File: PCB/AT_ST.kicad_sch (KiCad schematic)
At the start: 80 parts, among them J1 4PIN, J2 OLED, J3 Conn_01x05_Female, J4 Conn_01x05_Female, SW1 SW1, SW10 SW10, SW11 SW11, SW12 SW12, SW13 SW13, SW14 SW14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

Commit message: Updated some footprints.
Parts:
- R1, R2: footprint SofleKeyboard-footprint:R_1206_DoubleSided -> jw_custom_footprint:R_1206_DoubleSided
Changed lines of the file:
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@@
-    (stroke (width 0) (type default) (color 0 0 0 0))
-  )
-  (wire (pts (xy 42.418 71.628) (xy 42.418 73.787))
     (stroke (width 0) (type default) (color 0 0 0 0))
   )
@@
     (stroke (width 0) (type default) (color 0 0 0 0))
   )
+  (wire (pts (xy 42.418 71.628) (xy 46.99 71.628))
+    (stroke (width 0) (type default) (color 0 0 0 0))
+  )
   (wire (pts (xy 157.734 111.252) (xy 159.512 111.252))
     (stroke (width 0) (type default) (color 0 0 0 0))
@@
   )
   (wire (pts (xy 26.924 125.476) (xy 26.924 131.064))
+    (stroke (width 0) (type default) (color 0 0 0 0))
+  )
+  (wire (pts (xy 46.99 71.628) (xy 46.99 73.66))
     (stroke (width 0) (type default) (color 0 0 0 0))
   )
@@
     )
     (property "Value" "R" (id 1) (at 33.528 87.376 90))
-    (property "Footprint" "SofleKeyboard-footprint:R_1206_DoubleSided" (id 2) (at 33.528 85.598 90)
+    (property "Footprint" "jw_custom_footprint:R_1206_DoubleSided" (id 2) (at 33.528 85.598 90)
       (effects (font (size 1.27 1.27)) hide)
     )
@@
     )
     (property "Value" "R" (id 1) (at 33.528 82.804 90))
-    (property "Footprint" "SofleKeyboard-footprint:R_1206_DoubleSided" (id 2) (at 33.528 81.026 90)
+    (property "Footprint" "jw_custom_footprint:R_1206_DoubleSided" (id 2) (at 33.528 81.026 90)
       (effects (font (size 1.27 1.27)) hide)
     )
@@
     (pin "2")
   )
-  (symbol (lib_id "power:GND") (at 42.418 73.787 0) (unit 1)
-    (in_bom yes) (on_board yes)
-    (property "Reference" "#PWR0102" (id 0) (at 42.418 80.137 0)
-      (effects (font (size 1.27 1.27)) hide)
-    )
-    (property "Value" "GND" (id 1) (at 42.545 78.1812 0))
-    (property "Footprint" "" (id 2) (at 42.418 73.787 0)
-      (effects (font (size 1.27 1.27)) hide)
-    )
-    (property "Datasheet" "" (id 3) (at 42.418 73.787 0)
+  (symbol (lib_id "power:GND") (at 46.99 73.66 0) (unit 1)
+    (in_bom yes) (on_board yes)
+    (property "Reference" "#PWR0102" (id 0) (at 46.99 80.01 0)
+      (effects (font (size 1.27 1.27)) hide)
+    )
+    (property "Value" "GND" (id 1) (at 47.117 78.0542 0))
+    (property "Footprint" "" (id 2) (at 46.99 73.66 0)
+      (effects (font (size 1.27 1.27)) hide)
+    )
+    (property "Datasheet" "" (id 3) (at 46.99 73.66 0)
       (effects (font (size 1.27 1.27)) hide)
     )
@@
     )
     (path "/4f0dde52-9bad-44d4-aea8-222c0fca6124"
-      (reference "R1") (unit 1) (value "R") (footprint "SofleKeyboard-footprint:R_1206_DoubleSided")
+      (reference "R1") (unit 1) (value "R") (footprint "jw_custom_footprint:R_1206_DoubleSided")
     )
     (path "/401292cb-be96-4cb2-9cd9-a9fdf728011b"
-      (reference "R2") (unit 1) (value "R") (footprint "SofleKeyboard-footprint:R_1206_DoubleSided")
+      (reference "R2") (unit 1) (value "R") (footprint "jw_custom_footprint:R_1206_DoubleSided")
     )
     (path "/00000000-0000-0000-0000-00005b8ce7e7"

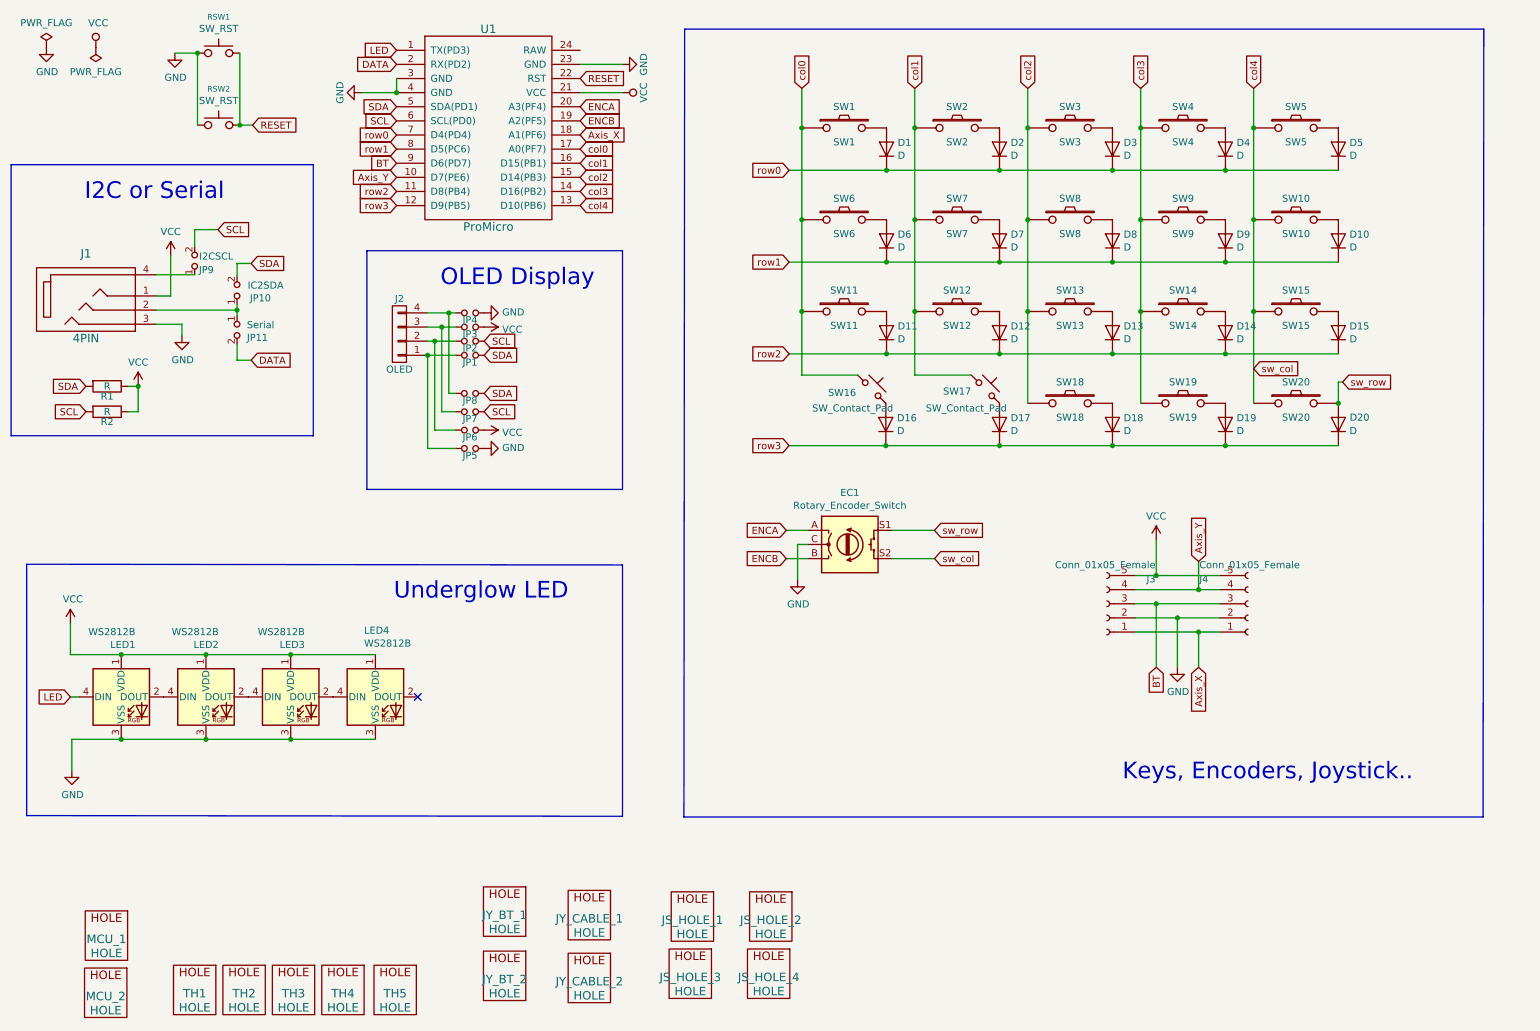
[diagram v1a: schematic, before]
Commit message: 1. Correct a serious pin allocation problem, where a digital pin was assigned for joystick Y axis. 2. Updated MX switches footprints. 3. Included flip style 5 pins FPC/FFC socket. 4. Minor changes here and there.
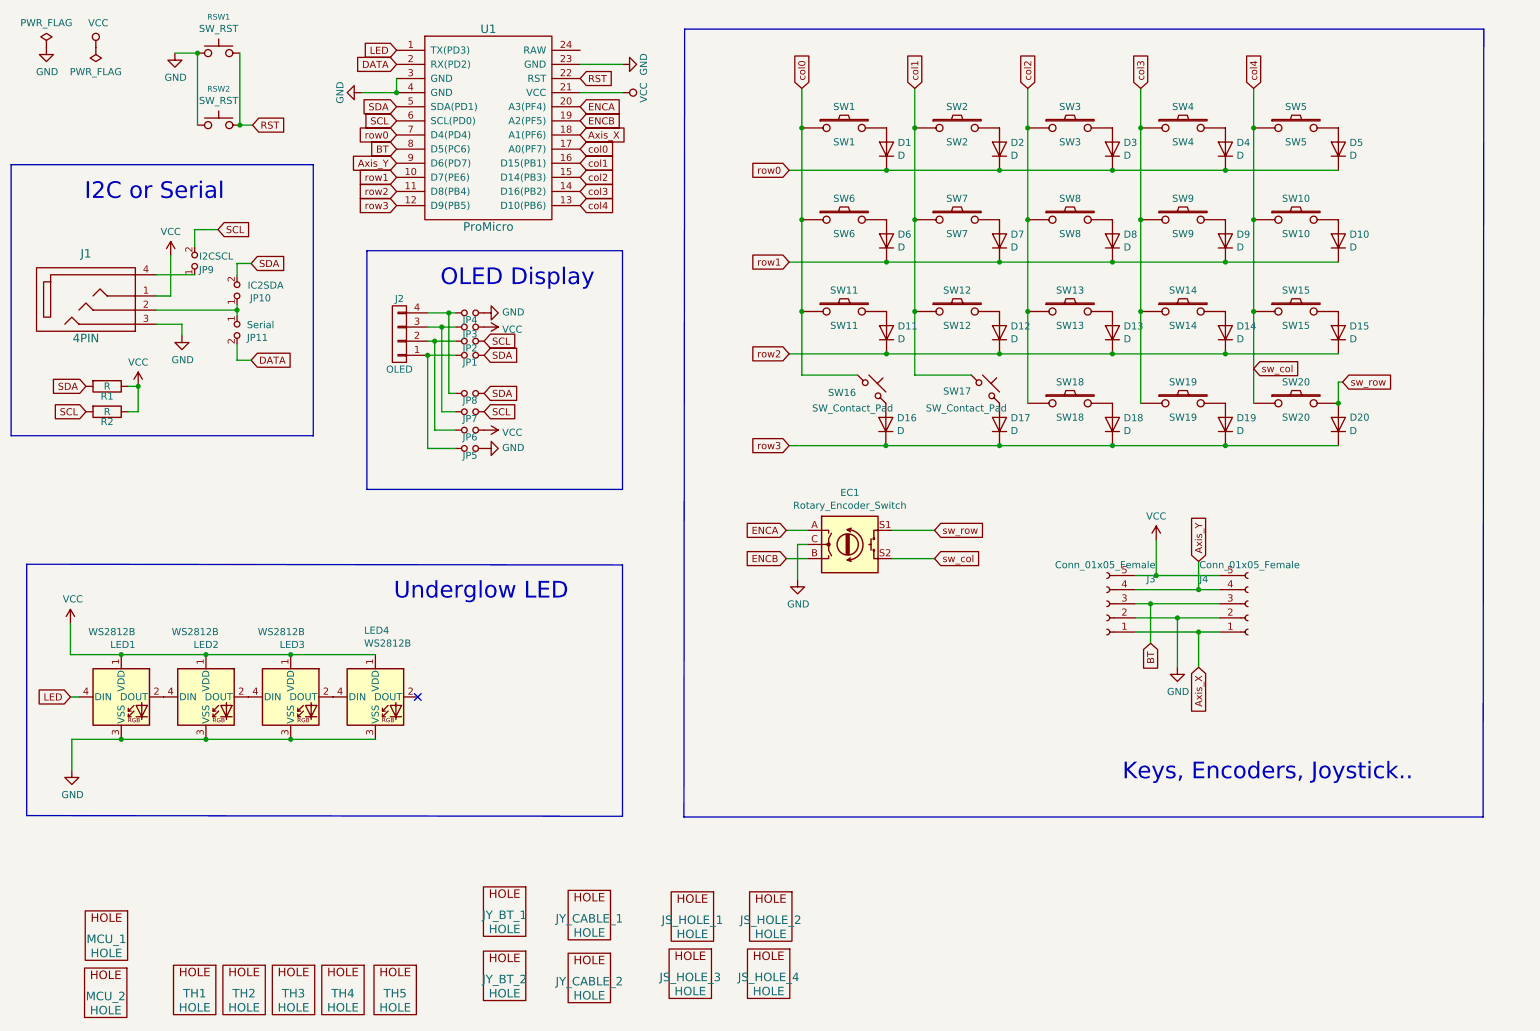
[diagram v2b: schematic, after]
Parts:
- D1, D10, D11, D12, D13, D14, D15, D16, D17, D18, D19, D2, D20, D3, D4, D5, D6, D7, D8, D9: footprint jw_custom_footprint:Diode_SOD123_THT -> jw_custom_footprint:Diode_SOD123_THT_2
- J3, J4: footprint Connector_FFC-FPC:TE_0-1734839-5_1x05-1MP_P0.5mm_Horizontal -> jw_custom_footprint:Molex_200528-0050_1x05-1MP_P0.5mm_Horizontal
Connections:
- net Axis_Y: now also U1.9 (D6(PD7)); no longer U1.10 (D7(PE6))
- net BT: now also U1.8 (D5(PC6)); no longer U1.9 (D6(PD7))
- net row1: now also U1.10 (D7(PE6)); no longer U1.8 (D5(PC6))
- net RESET renamed RST
